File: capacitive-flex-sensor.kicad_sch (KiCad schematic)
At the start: 92 parts, among them J3 Conn_01x12, J4 Conn_01x12

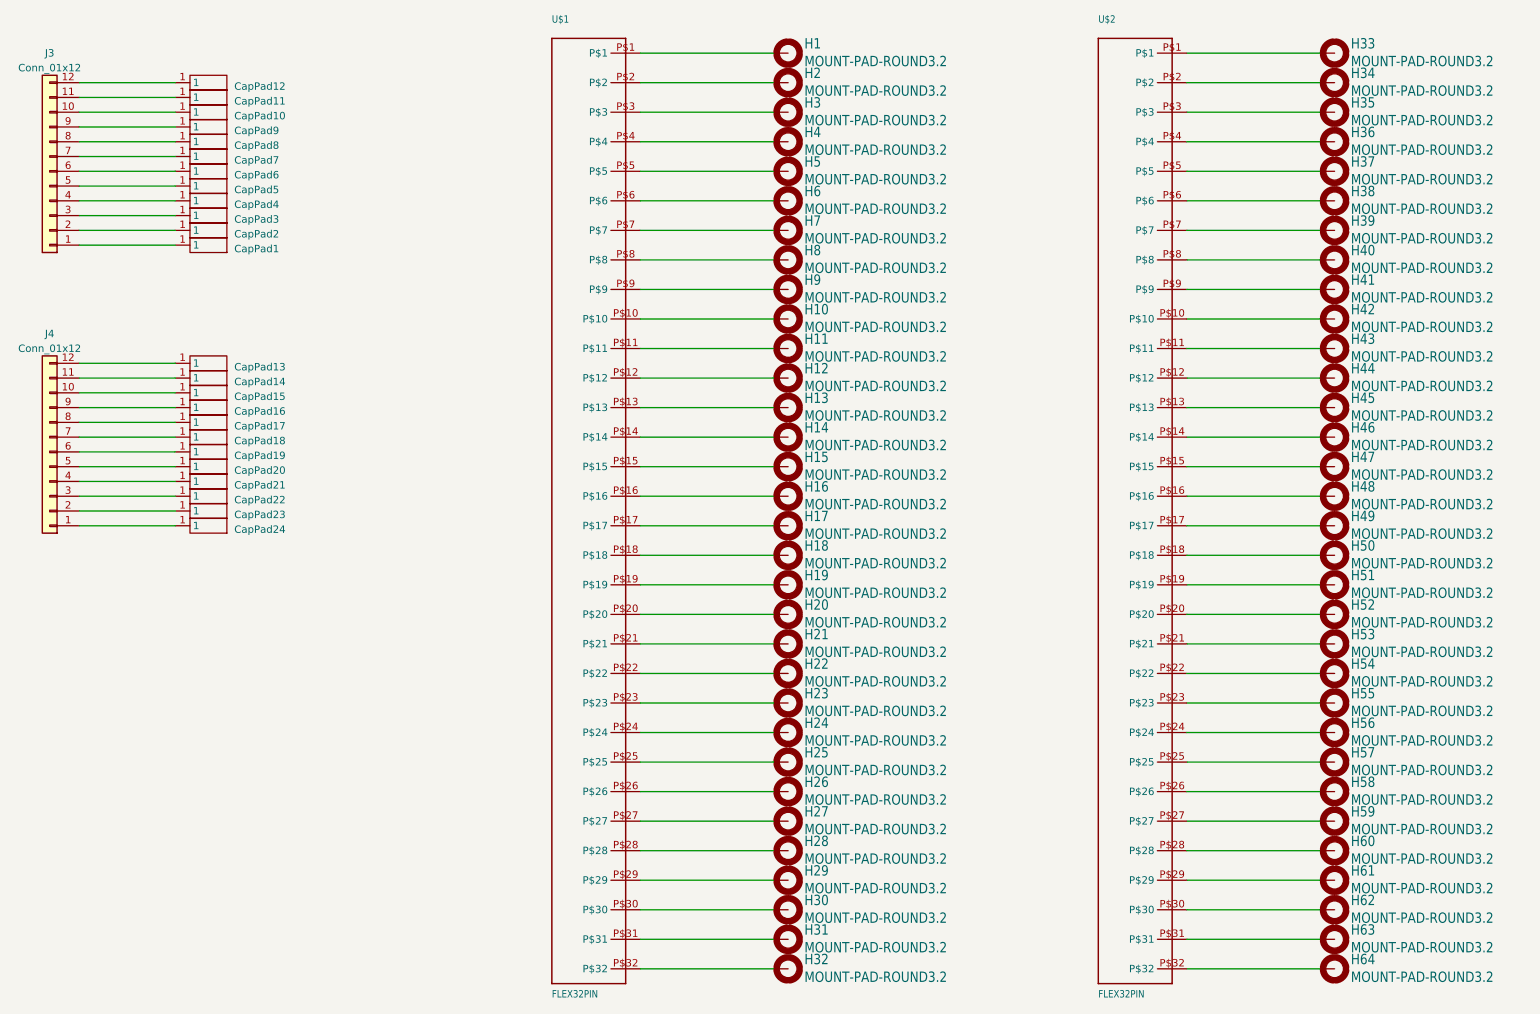
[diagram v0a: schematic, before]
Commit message: feat: new version with 5 pads and pins on top
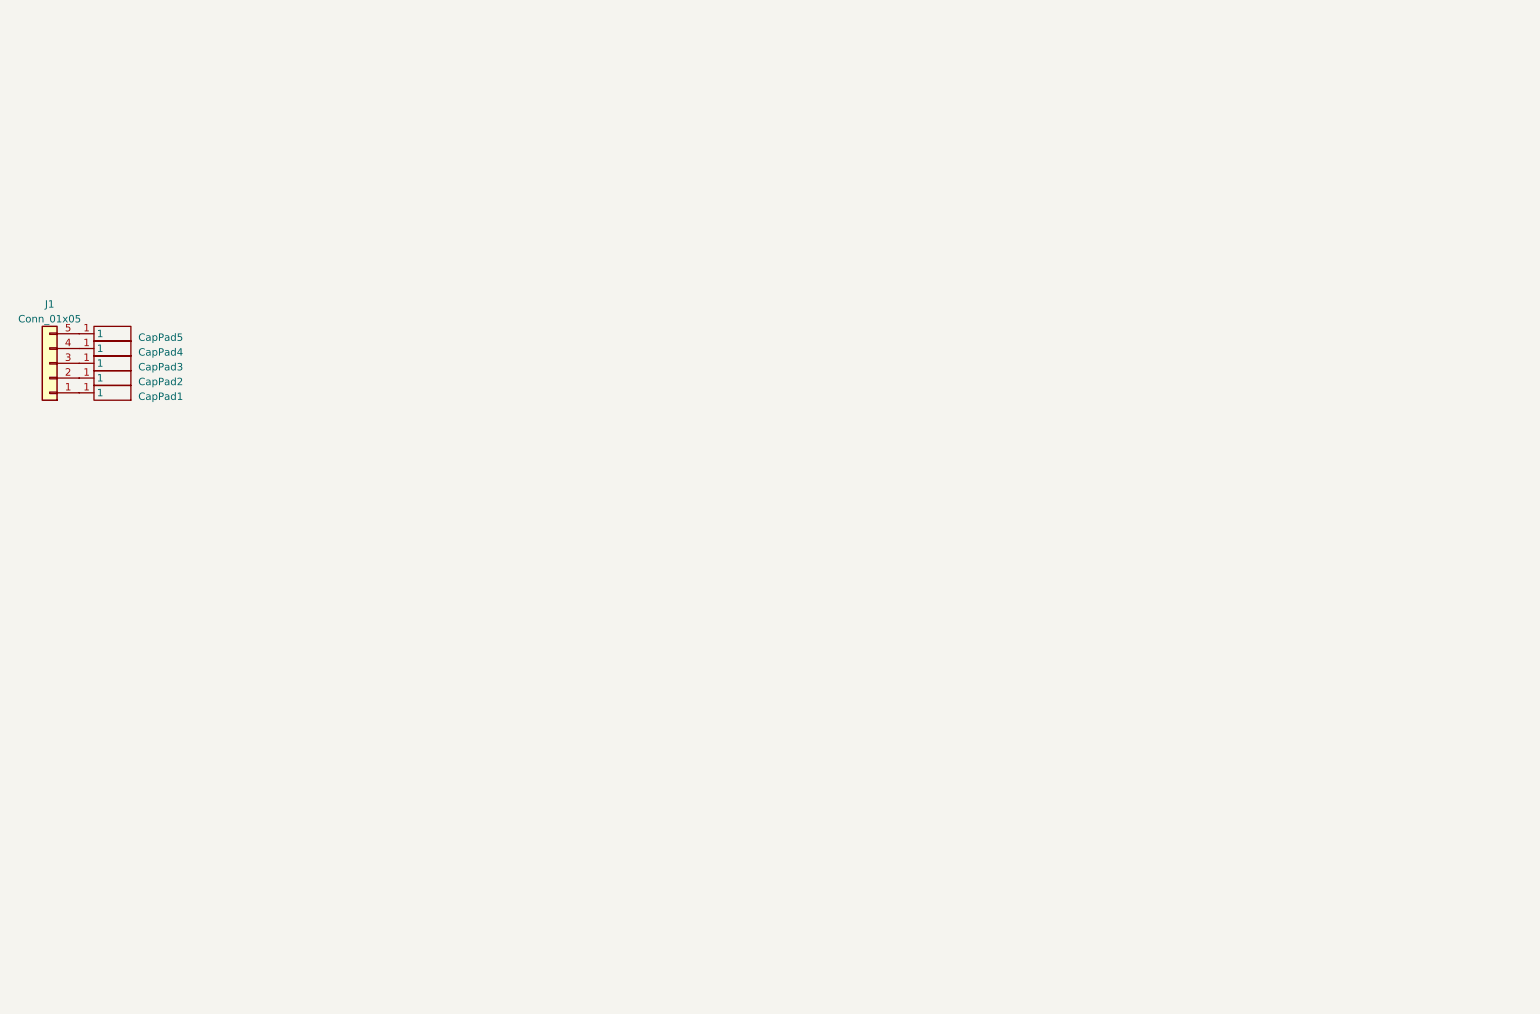
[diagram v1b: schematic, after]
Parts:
- removed CapPad10, CapPad11, CapPad12, CapPad13, CapPad14, CapPad15, CapPad16, CapPad17, CapPad18, CapPad19, CapPad20, CapPad21, CapPad22, CapPad23, CapPad24, CapPad6, CapPad7, CapPad8, CapPad9: ~, Sensor_Capacitive:capacitive_pad_40x17.5, symbol Sensor_Capacitive:capacitive_pad_40x20
- removed H1, H10, H11, H12, H13, H14, H15, H16, H17, H18, H19, H2, H20, H21, H22, H23, H24, H25, H26, H27, H28, H29, H3, H30, H31, H32, H33, H34, H35, H36, H37, H38, H39, H4, H40, H41, H42, H43, H44, H45, H46, H47, H48, H49, H5, H50, H51, H52, H53, H54, H55, H56, H57, H58, H59, H6, H60, H61, H62, H63, H64, H7, H8, H9: MOUNT-PAD-ROUND3.2, flex-1D-V7:3,2-PAD, symbol flex-1D-V7-eagle-import:MOUNT-PAD-ROUND3.2
- removed J3, J4: Conn_01x12, Connector_PinHeader_2.54mm:PinHeader_1x12_P2.54mm_Vertical, symbol Connector_Generic:Conn_01x12
- removed U$1, U$2: FLEX32PIN, flex-1D-V7:FLEX32PIN, symbol flex-1D-V7-eagle-import:FLEX32PIN
- added J1: Conn_01x05, Connector_PinHeader_2.54mm:PinHeader_1x05_P2.54mm_Vertical, symbol Connector_Generic:Conn_01x05
- CapPad1, CapPad2, CapPad3, CapPad4, CapPad5: footprint Sensor_Capacitive:capacitive_pad_40x17.5 -> Sensor_Capacitive:capacitive_pad_20x20
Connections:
- net at CapPad2.1: now also J1.2 (Pin_2)
- net at CapPad5.1: now also J1.5 (Pin_5)
- net at CapPad4.1: now also J1.4 (Pin_4)
- net at CapPad1.1: now also J1.1 (Pin_1)
- net at CapPad3.1: now also J1.3 (Pin_3)
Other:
- moved on the sheet: CapPad1, CapPad2, CapPad3, CapPad4, CapPad5
